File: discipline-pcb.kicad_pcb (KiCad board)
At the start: 2 copper layers, 304.9 x 122.8 mm, 185 parts, among them J1 AVR-ISP-6, SW1 KEYSW, SW10 KEYSW, SW11 KEYSW, SW12 KEYSW, SW13 KEYSW, SW14 KEYSW, SW15 Rotary_Encoder_Switch, SW16 KEYSW, SW17 KEYSW, SW18 KEYSW, SW19 KEYSW, SW2 KEYSW, SW20 KEYSW, SW21 KEYSW, SW22 KEYSW, SW23 KEYSW, SW24 KEYSW, SW25 KEYSW, SW26 KEYSW, SW27 KEYSW, SW28 KEYSW, SW29 KEYSW, SW3 KEYSW, SW30 KEYSW, SW31 KEYSW, SW32 KEYSW, SW33 KEYSW, SW34 KEYSW, SW35 KEYSW, SW36 KEYSW, SW37 KEYSW, SW38 KEYSW, SW39 KEYSW, SW4 KEYSW, SW40 KEYSW, SW41 KEYSW, SW42 KEYSW, SW43 KEYSW, SW44 KEYSW, SW45 KEYSW, SW46 KEYSW, SW47 KEYSW, SW48 KEYSW, SW49 KEYSW, SW5 KEYSW, SW50 KEYSW, SW51 KEYSW, SW52 KEYSW, SW53 KEYSW, SW54 KEYSW, SW55 KEYSW, SW56 KEYSW, SW57 KEYSW, SW58 KEYSW, SW59 KEYSW, SW6 KEYSW, SW60 KEYSW, SW61 KEYSW, SW62 KEYSW, SW63 KEYSW, SW64 KEYSW, SW65 KEYSW, SW66 KEYSW, SW67 KEYSW, SW68 KEYSW, SW69 KEYSW, SW7 KEYSW, SW70 KEYSW, SW71 KEYSW, SW72 KEYSW, SW73 KEYSW, SW74 KEYSW, SW8 KEYSW, SW9 KEYSW, U1 ATmega32A-PU, Y1 Crystal

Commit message: added 3x1u and 2x1.5u options in bottom right modifier section. renumbered switches and diodes
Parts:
- added D65: , cftkb:D_DO-35_SOD27_P5.08mm_Horizontal, F.Cu at (250.3, 71.1)
- added SW67: KEYSW, cftkb:SW_Cherry_MX1A_1.00u_PCB-NOSCREEN, F.Cu at (294.5, 165.9)
- added SW76: KEYSW-keyboard_parts, cftkb:SW_Cherry_MX1A_1.25u_PCBNOSCREEN, F.Cu at (258.8, 165.9)
- added SW77: KEYSW-keyboard_parts, cftkb:SW_Cherry_MX1A_1.50u_PCBNOSCREEN, F.Cu at (261.2, 165.9)
- added SW78: KEYSW-keyboard_parts, cftkb:SW_Cherry_MX1A_1.25u_PCBNOSCREEN, F.Cu at (282.5, 165.9)
- added SW79: KEYSW-keyboard_parts, cftkb:SW_Cherry_MX1A_1.50u_PCBNOSCREEN, F.Cu at (289.7, 165.9)
- SW65: value KEYSW -> KEYSW-keyboard_parts; footprint cftkb:SW_Cherry_MX1A_1.25u_PCBNOSCREEN -> cftkb:SW_Cherry_MX1A_1.00u_PCB-NOSCREEN
- SW66: footprint cftkb:SW_Cherry_MX1A_1.25u_PCBNOSCREEN -> cftkb:SW_Cherry_MX1A_1.00u_PCB-NOSCREEN
- moved D61 185.9 mm to (101.4, 166.9)
- moved SW66 7.31 mm to (275.5, 166.0)
- moved D64 5.78 mm to (253.4, 66.2)
- moved D63 3.60 mm to (256.7, 67.7)
- moved D62 3.50 mm to (259.8, 69.5)
- moved SW65 2.41 mm to (256.4, 166.0)
- renumbered D65 to D66, D66 to D67, D67 to D68, D68 to D69, D69 to D70, D70 to D71, D71 to D72, SW67 to SW68, SW68 to SW69, SW69 to SW70, SW74 to SW71, SW70 to SW72, SW71 to SW73, SW73 to SW74, SW72 to SW75
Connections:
- D66 pad 2: Net-(D65-Pad2) -> Net-(D66-Pad2)
- D67 pad 2: Net-(D66-Pad2) -> Net-(D67-Pad2)
- SW65 pad 1: col10 -> col9
- SW66 pad 1: col11 -> col10
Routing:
- net Net-(D61-Pad2): track 401.4 -> 10.1 mm
- net Net-(D67-Pad2): track 0.00 -> 319.1 mm
- net Net-(D65-Pad2): track 395.5 -> 277.6 mm
- net Net-(D66-Pad2): track 332.6 -> 391.9 mm
- net col9: track 220.7 -> 252.3 mm
- net row4: track 429.8 -> 455.6 mm
- net col10: track 220.7 -> 241.9 mm
- net col11: track 200.2 -> 204.8 mm
- net Net-(D63-Pad2): track 349.4 -> 351.8 mm
- net (no net): track 0.00 -> 1.20 mm
- net Net-(D62-Pad2): track 376.4 -> 377.5 mm

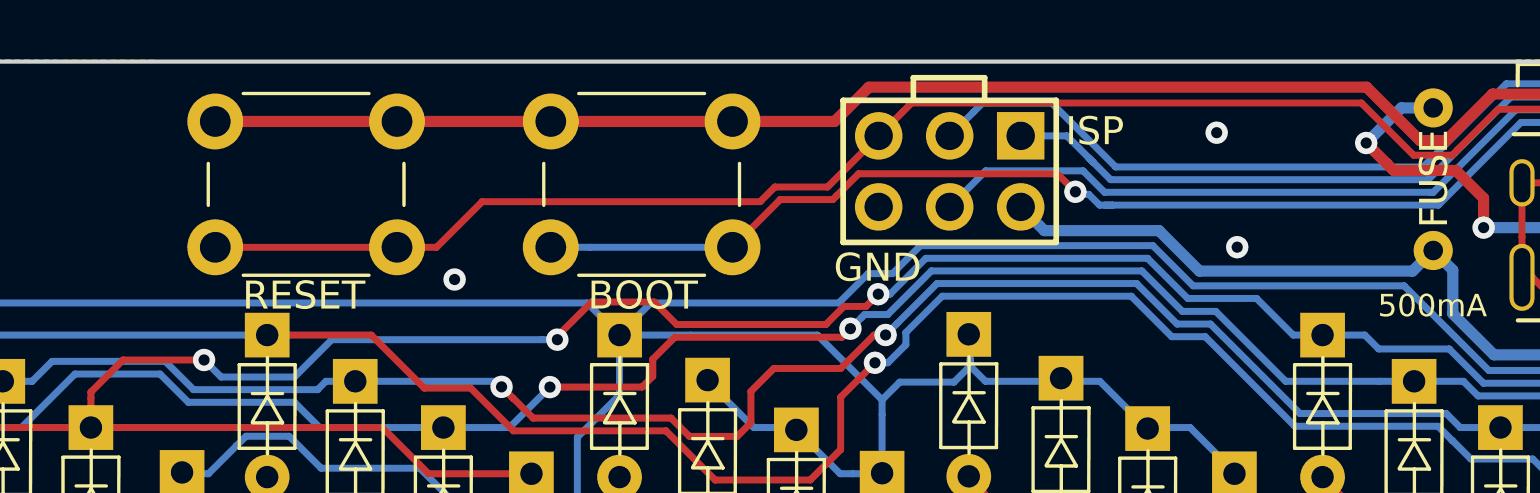
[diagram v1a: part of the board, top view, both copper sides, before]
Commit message: replaced reset and boot buttons with right angle buttons
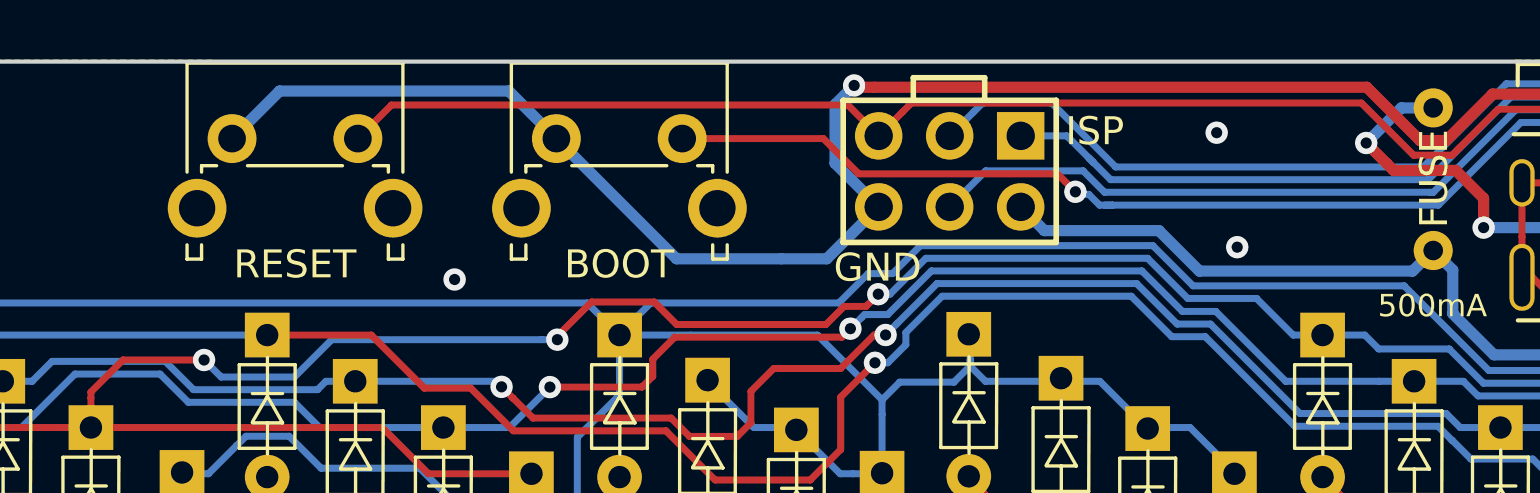
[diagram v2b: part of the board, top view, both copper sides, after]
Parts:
- BOOT1, RESET1: footprint cftkb:SW_PUSH_6mm -> Button_Switch_THT:SW_Tactile_SPST_Angled_PTS645Vx31-2LFS
- moved RESET1 0.86 mm to (227.1, 60.4)
- moved BOOT1 0.64 mm to (238.7, 60.4)
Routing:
- net GND: track 223.5 -> 232.5 mm, vias 38 -> 39
- net boot: track 120.6 -> 114.5 mm
- net reset: track 126.8 -> 121.0 mm
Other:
- board text added: "BOOT"

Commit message: change to fix fills
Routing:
- net row4: track 455.6 -> 457.4 mm, vias 0 -> 1

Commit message: reducing number of screws and changing placements
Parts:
- removed the REF** at (206.2, 103.8)
- removed the REF** at (301.4, 103.8)
- removed the REF** at (110.9, 103.8)
- removed the REF** at (320.5, 161.8)
- removed the REF** at (101.4, 161.9)
- added REF**: MountingHole_2.2mm_M2_Pad, MountingHole:MountingHole_2.2mm_M2_Pad, F.Cu at (316.2, 151.9)
- added REF**: MountingHole_2.2mm_M2_Pad, MountingHole:MountingHole_2.2mm_M2_Pad, F.Cu at (94.1, 151.9)
- moved REF** 9.00 mm to (199.6, 170.9)
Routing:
- net col1: track 315.5 -> 316.4 mm
